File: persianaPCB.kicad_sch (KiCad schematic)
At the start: 0 parts

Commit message: avance en SCH
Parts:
- added H1, H2, H3, H4: MountingHole, MountingHole:MountingHole_4.3mm_M4, symbol Mechanical:MountingHole
- added J1: BORNERA-2, TerminalBlock_Phoenix:TerminalBlock_Phoenix_MKDS-1,5-2-5.08_1x02_P5.08mm_Horizontal, symbol Connector:Screw_Terminal_01x02
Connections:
- new net GND: J1.2 (Pin_2)
- new net fuente/VIN: J1.1 (Pin_1)
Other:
- added sheet core (core.kicad_sch)
- added sheet entradas (entradas.kicad_sch)
- added sheet salidas (salidas.kicad_sch)
- sheet fuente ports: added 3.3V, 5V, GND, VIN; removed none

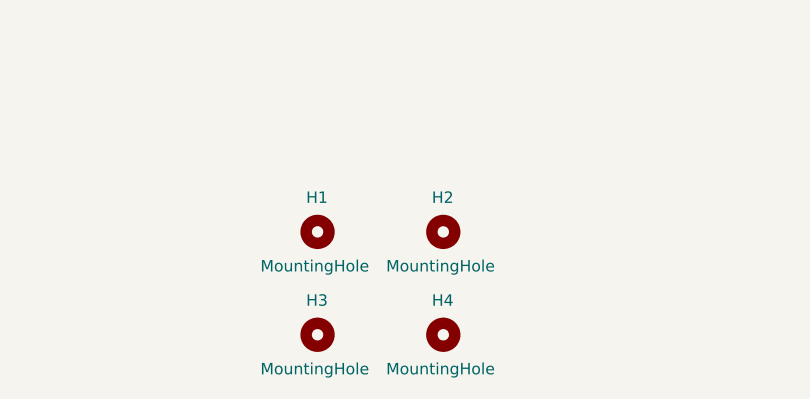
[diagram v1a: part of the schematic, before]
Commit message: cambios en tamaño y agujeros de fijación
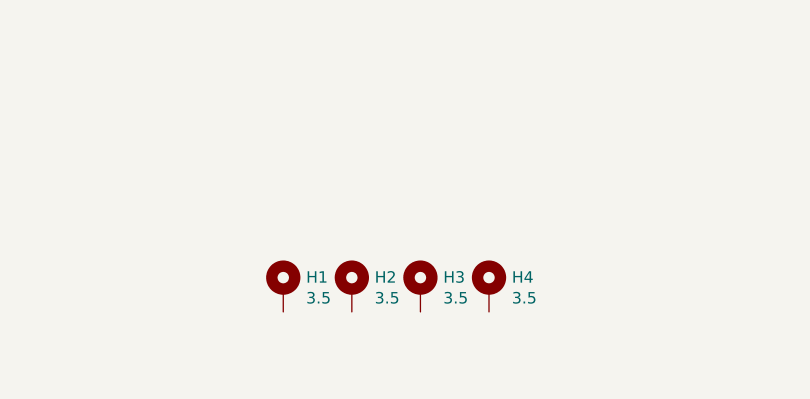
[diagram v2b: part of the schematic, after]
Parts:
- removed H1, H2, H3, H4: MountingHole, MountingHole:MountingHole_4.3mm_M4, symbol Mechanical:MountingHole
- added H1, H2, H3, H4: 3.5, MountingHole:MountingHole_3.5mm_Pad, symbol Mechanical:MountingHole_Pad
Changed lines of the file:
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@@
+    (pin "1")
+  )
+  (symbol (lib_id "Mechanical:MountingHole_Pad") (at 100.33 179.07 0) (unit 1)
+    (in_bom yes) (on_board yes)
+    (property "Reference" "H1" (id 0) (at 102.87 177.7746 0)
+      (effects (font (size 1.27 1.27)) (justify left))
+    )
+    (property "Value" "3.5" (id 1) (at 102.87 180.086 0)
+      (effects (font (size 1.27 1.27)) (justify left))
+    )
+    (property "Footprint" "MountingHole:MountingHole_3.5mm_Pad" (id 2) (at 100.33 179.07 0)
+      (effects (font (size 1.27 1.27)) hide)
+    )
+    (property "Datasheet" "~" (id 3) (at 100.33 179.07 0)
+      (effects (font (size 1.27 1.27)) hide)
+    )
     (pin "1")
   )
@@
     (pin "1")
   )
-  (symbol (lib_id "Mechanical:MountingHole") (at 104.14 184.15 0) (unit 1)
+  (symbol (lib_id "Mechanical:MountingHole_Pad") (at 123.19 179.07 0) (unit 1)
     (in_bom yes) (on_board yes)
-    (property "Reference" "H3" (id 0) (at 102.87 180.34 0)
-      (effects (font (size 1.27 1.27)) (justify left))
-    )
-    (property "Value" "MountingHole" (id 1) (at 97.79 187.96 0)
-      (effects (font (size 1.27 1.27)) (justify left))
-    )
-    (property "Footprint" "MountingHole:MountingHole_4.3mm_M4" (id 2) (at 104.14 184.15 0)
-      (effects (font (size 1.27 1.27)) hide)
-    )
-    (property "Datasheet" "~" (id 3) (at 104.14 184.15 0)
-      (effects (font (size 1.27 1.27)) hide)
-    )
+    (property "Reference" "H4" (id 0) (at 125.73 177.7746 0)
+      (effects (font (size 1.27 1.27)) (justify left))
+    )
+    (property "Value" "3.5" (id 1) (at 125.73 180.086 0)
+      (effects (font (size 1.27 1.27)) (justify left))
+    )
+    (property "Footprint" "MountingHole:MountingHole_3.5mm_Pad" (id 2) (at 123.19 179.07 0)
+      (effects (font (size 1.27 1.27)) hide)
+    )
+    (property "Datasheet" "~" (id 3) (at 123.19 179.07 0)
+      (effects (font (size 1.27 1.27)) hide)
+    )
+    (pin "1")
+  )
+  (symbol (lib_id "Mechanical:MountingHole_Pad") (at 107.95 179.07 0) (unit 1)
+    (in_bom yes) (on_board yes)
+    (property "Reference" "H2" (id 0) (at 110.49 177.7746 0)
+      (effects (font (size 1.27 1.27)) (justify left))
+    )
+    (property "Value" "3.5" (id 1) (at 110.49 180.086 0)
+      (effects (font (size 1.27 1.27)) (justify left))
+    )
+    (property "Footprint" "MountingHole:MountingHole_3.5mm_Pad" (id 2) (at 107.95 179.07 0)
+      (effects (font (size 1.27 1.27)) hide)
+    )
+    (property "Datasheet" "~" (id 3) (at 107.95 179.07 0)
+      (effects (font (size 1.27 1.27)) hide)
+    )
+    (pin "1")
   )
   (symbol (lib_id "power:GND") (at 68.58 134.62 0) (unit 1)
@@
     (pin "1")
   )
-  (symbol (lib_id "Mechanical:MountingHole") (at 118.11 172.72 0) (unit 1)
-    (in_bom yes) (on_board yes)
-    (property "Reference" "H2" (id 0) (at 116.84 168.91 0)
-      (effects (font (size 1.27 1.27)) (justify left))
-    )
-    (property "Value" "MountingHole" (id 1) (at 111.76 176.53 0)
-      (effects (font (size 1.27 1.27)) (justify left))
-    )
-    (property "Footprint" "MountingHole:MountingHole_4.3mm_M4" (id 2) (at 118.11 172.72 0)
-      (effects (font (size 1.27 1.27)) hide)
-    )
-    (property "Datasheet" "~" (id 3) (at 118.11 172.72 0)
-      (effects (font (size 1.27 1.27)) hide)
-    )
-  )
   (symbol (lib_id "power:GND") (at 157.48 134.62 0) (unit 1)
     (in_bom yes) (on_board yes) (fields_autoplaced)
@@
     (pin "1")
   )
-  (symbol (lib_id "Mechanical:MountingHole") (at 104.14 172.72 0) (unit 1)
+  (symbol (lib_id "Mechanical:MountingHole_Pad") (at 115.57 179.07 0) (unit 1)
     (in_bom yes) (on_board yes)
-    (property "Reference" "H1" (id 0) (at 102.87 168.91 0)
-      (effects (font (size 1.27 1.27)) (justify left))
-    )
-    (property "Value" "MountingHole" (id 1) (at 97.79 176.53 0)
-      (effects (font (size 1.27 1.27)) (justify left))
-    )
-    (property "Footprint" "MountingHole:MountingHole_4.3mm_M4" (id 2) (at 104.14 172.72 0)
-      (effects (font (size 1.27 1.27)) hide)
-    )
-    (property "Datasheet" "~" (id 3) (at 104.14 172.72 0)
-      (effects (font (size 1.27 1.27)) hide)
-    )
-  )
-  (symbol (lib_id "Mechanical:MountingHole") (at 118.11 184.15 0) (unit 1)
-    (in_bom yes) (on_board yes)
-    (property "Reference" "H4" (id 0) (at 116.84 180.34 0)
-      (effects (font (size 1.27 1.27)) (justify left))
-    )
-    (property "Value" "MountingHole" (id 1) (at 111.76 187.96 0)
-      (effects (font (size 1.27 1.27)) (justify left))
-    )
-    (property "Footprint" "MountingHole:MountingHole_4.3mm_M4" (id 2) (at 118.11 184.15 0)
-      (effects (font (size 1.27 1.27)) hide)
-    )
-    (property "Datasheet" "~" (id 3) (at 118.11 184.15 0)
-      (effects (font (size 1.27 1.27)) hide)
-    )
+    (property "Reference" "H3" (id 0) (at 118.11 177.7746 0)
+      (effects (font (size 1.27 1.27)) (justify left))
+    )
+    (property "Value" "3.5" (id 1) (at 118.11 180.086 0)
+      (effects (font (size 1.27 1.27)) (justify left))
+    )
+    (property "Footprint" "MountingHole:MountingHole_3.5mm_Pad" (id 2) (at 115.57 179.07 0)
+      (effects (font (size 1.27 1.27)) hide)
+    )
+    (property "Datasheet" "~" (id 3) (at 115.57 179.07 0)
+      (effects (font (size 1.27 1.27)) hide)
+    )
+    (pin "1")
   )
   (symbol (lib_id "Connector:Screw_Terminal_01x02") (at 118.11 27.94 0) (unit 1)
@@
       (reference "D6") (unit 1) (value "SM4007") (footprint "Diode_SMD:D_MELF")
     )
-    (path "/d1b1f18c-92a0-4818-a2db-f181a454a4f7"
-      (reference "H1") (unit 1) (value "MountingHole") (footprint "MountingHole:MountingHole_4.3mm_M4")
-    )
-    (path "/8755ac09-32e9-4a4b-ad83-b0b79dd615f0"
-      (reference "H2") (unit 1) (value "MountingHole") (footprint "MountingHole:MountingHole_4.3mm_M4")
-    )
-    (path "/62442c5f-42a1-4e50-8535-1d5a834e2277"
-      (reference "H3") (unit 1) (value "MountingHole") (footprint "MountingHole:MountingHole_4.3mm_M4")
-    )
-    (path "/e3457c24-ea9d-475e-bd44-815ab91ee95d"
-      (reference "H4") (unit 1) (value "MountingHole") (footprint "MountingHole:MountingHole_4.3mm_M4")
+    (path "/34a585d8-d3ba-47bc-ac3d-ed567a1fea89"
+      (reference "H1") (unit 1) (value "3.5") (footprint "MountingHole:MountingHole_3.5mm_Pad")
+    )
+    (path "/64302057-935d-468f-88b9-59aee71191ce"
+      (reference "H2") (unit 1) (value "3.5") (footprint "MountingHole:MountingHole_3.5mm_Pad")
+    )
+    (path "/f2524ef6-65af-4120-ab0c-2e36c8ac5f7b"
+      (reference "H3") (unit 1) (value "3.5") (footprint "MountingHole:MountingHole_3.5mm_Pad")
+    )
+    (path "/5b1af344-c6c7-47c4-b3b6-b8301dd675ab"
+      (reference "H4") (unit 1) (value "3.5") (footprint "MountingHole:MountingHole_3.5mm_Pad")
     )
     (path "/f66fc17d-6daf-4ead-8f5f-83eb18d2c778"

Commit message: avance en PCB y SCH
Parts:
- H1, H2, H3, H4: value 3.5 -> 4mm; footprint MountingHole:MountingHole_3.5mm_Pad -> MountingHole:MountingHole_4mm_Pad
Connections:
- net GND: now also J1.1 (Pin_1); no longer J1.2 (Pin_2)
- net fuente/VIN: now also J1.2 (Pin_2); no longer J1.1 (Pin_1)
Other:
- sheet entradas ports: added +VSW; removed none
- sheet fuente ports: added +VSW; removed none
- moved on the sheet: J1

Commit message: avance en PCB y SCH
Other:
- sheet core ports: added GPIO14, GPIO16; removed GPIO4, GPIO5
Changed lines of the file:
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@@
       (effects (font (size 1.27 1.27)) (justify left))
     )
-    (pin "GPIO4" bidirectional (at 129.54 95.25 180)
+    (pin "GPIO12" bidirectional (at 185.42 95.25 0)
+      (effects (font (size 1.27 1.27)) (justify right))
+    )
+    (pin "GPIO13" bidirectional (at 185.42 97.79 0)
+      (effects (font (size 1.27 1.27)) (justify right))
+    )
+    (pin "GPIO16" bidirectional (at 129.54 95.25 180)
       (effects (font (size 1.27 1.27)) (justify left))
     )
-    (pin "GPIO5" bidirectional (at 129.54 97.79 180)
+    (pin "GPIO14" bidirectional (at 129.54 97.79 180)
       (effects (font (size 1.27 1.27)) (justify left))
-    )
-    (pin "GPIO12" bidirectional (at 185.42 95.25 0)
-      (effects (font (size 1.27 1.27)) (justify right))
-    )
-    (pin "GPIO13" bidirectional (at 185.42 97.79 0)
-      (effects (font (size 1.27 1.27)) (justify right))
     )
   )
@@
     )
     (path "/77300f17-b1b3-4d4c-b2e0-f042e713f706/d778ded5-9c60-4ed6-b112-22e23a12f963"
-      (reference "U2") (unit 1) (value "LM1117-3.3") (footprint "Package_TO_SOT_SMD:TO-252-3_TabPin2")
+      (reference "U2") (unit 1) (value "LM1117-3.3") (footprint "Package_TO_SOT_SMD:SOT-223-3_TabPin2")
     )
     (path "/67d1a537-0191-48d8-8448-e2071330e71a/45e61188-bec6-4d1d-a05c-e61ab5ee1315"

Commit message: avances finales
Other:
- sheet core ports: added GPIO4, GPIO5; removed GPIO12, GPIO16
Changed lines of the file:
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@@
       (effects (font (size 1.27 1.27)) (justify left))
     )
-    (pin "GPIO12" bidirectional (at 185.42 95.25 0)
-      (effects (font (size 1.27 1.27)) (justify right))
-    )
-    (pin "GPIO13" bidirectional (at 185.42 97.79 0)
-      (effects (font (size 1.27 1.27)) (justify right))
-    )
-    (pin "GPIO16" bidirectional (at 129.54 95.25 180)
+    (pin "GPIO14" bidirectional (at 129.54 95.25 180)
       (effects (font (size 1.27 1.27)) (justify left))
     )
-    (pin "GPIO14" bidirectional (at 129.54 97.79 180)
+    (pin "GPIO13" bidirectional (at 129.54 97.79 180)
       (effects (font (size 1.27 1.27)) (justify left))
+    )
+    (pin "GPIO4" bidirectional (at 185.42 97.79 0)
+      (effects (font (size 1.27 1.27)) (justify right))
+    )
+    (pin "GPIO5" bidirectional (at 185.42 95.25 0)
+      (effects (font (size 1.27 1.27)) (justify right))
     )
   )
@@
       (reference "#PWR0104") (unit 1) (value "+VSW") (footprint "")
     )
+    (path "/67d1a537-0191-48d8-8448-e2071330e71a/76e69ec2-ea30-4cf6-bec7-bd3ab33574a7"
+      (reference "#PWR0105") (unit 1) (value "GND") (footprint "")
+    )
+    (path "/67d1a537-0191-48d8-8448-e2071330e71a/3c181f81-b776-4adc-baf5-24e4927b80f1"
+      (reference "#PWR0106") (unit 1) (value "+3.3V") (footprint "")
+    )
     (path "/77300f17-b1b3-4d4c-b2e0-f042e713f706/15a9c483-2893-49bb-a97f-aaa7e30f3258"
       (reference "C1") (unit 1) (value "4,7nF") (footprint "Capacitor_SMD:C_0805_2012Metric_Pad1.18x1.45mm_HandSolder")
@@
       (reference "C8") (unit 1) (value "100nF 50V") (footprint "Capacitor_SMD:C_0805_2012Metric_Pad1.18x1.45mm_HandSolder")
     )
-    (path "/67d1a537-0191-48d8-8448-e2071330e71a/47e4052a-c4f5-4fd8-a0b1-e9df9a45ea8d"
-      (reference "C9") (unit 1) (value "4,7uF") (footprint "Capacitor_SMD:C_0805_2012Metric_Pad1.18x1.45mm_HandSolder")
-    )
     (path "/67d1a537-0191-48d8-8448-e2071330e71a/ffca6f22-ee74-4060-9bcc-9533a5653c5f"
       (reference "C10") (unit 1) (value "4,7uF") (footprint "Capacitor_SMD:C_0805_2012Metric_Pad1.18x1.45mm_HandSolder")
@@
       (reference "R13") (unit 1) (value "1K") (footprint "Resistor_SMD:R_0805_2012Metric_Pad1.20x1.40mm_HandSolder")
     )
+    (path "/67d1a537-0191-48d8-8448-e2071330e71a/2389e7fc-1cf8-4473-a08a-6b090a91ae7c"
+      (reference "R14") (unit 1) (value "10K") (footprint "Resistor_SMD:R_0805_2012Metric_Pad1.20x1.40mm_HandSolder")
+    )
+    (path "/67d1a537-0191-48d8-8448-e2071330e71a/68bd6e62-71eb-4a2d-856d-a9dfa6edaf7b"
+      (reference "R15") (unit 1) (value "10K") (footprint "Resistor_SMD:R_0805_2012Metric_Pad1.20x1.40mm_HandSolder")
+    )
     (path "/67d1a537-0191-48d8-8448-e2071330e71a/c21d2378-d84a-4389-a278-beae705eadc1"

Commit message: avance final!
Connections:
- no-connect marks 0 -> 4
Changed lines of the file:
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@@
   (junction (at 156.21 72.39) (diameter 0) (color 0 0 0 0)
   )
+  (no_connect (at 100.33 181.61))
+  (no_connect (at 123.19 181.61))
+  (no_connect (at 115.57 181.61))
+  (no_connect (at 107.95 181.61))
   (wire (pts (xy 156.21 46.99) (xy 156.21 72.39))
     (stroke (width 0) (type default) (color 0 0 0 0))
